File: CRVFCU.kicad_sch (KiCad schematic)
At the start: 161 parts, among them J1 TagConnect_TC2030, J2 Conn_01x02, J3 USB_C_Receptacle_USB2.0_16P, J4 Micro_SD_Card_Det2, J5 Conn_01x02, Q3 DMG2301L, Q4 BC818, Q5 DMG2301L, Q6 DMG2301L, U1 MS5611-01BA, U10 W25Q128JVS, U11 EClamp2515K, U12 ESDALC6V1W5, U13 USBLC6-2SC6, U14 USBLC6-2SC6, U15 MAX17049, U16 SI7232DN-T1, U17 SN74LV1T34DCK, U18 AP63205WU, U2 STM32H747IITx, U3 LIS2MDL, U4 ICM-45686, U5 FXMA108, U7 LDL1117S33R, U8 SI7232DN-T1, U9 USBLC6-4SC6, Y1 ECS-.327-6-34QCS-TR, Y2 ECS-250-10-33B-CKY-TR3, Y3 32.768khz

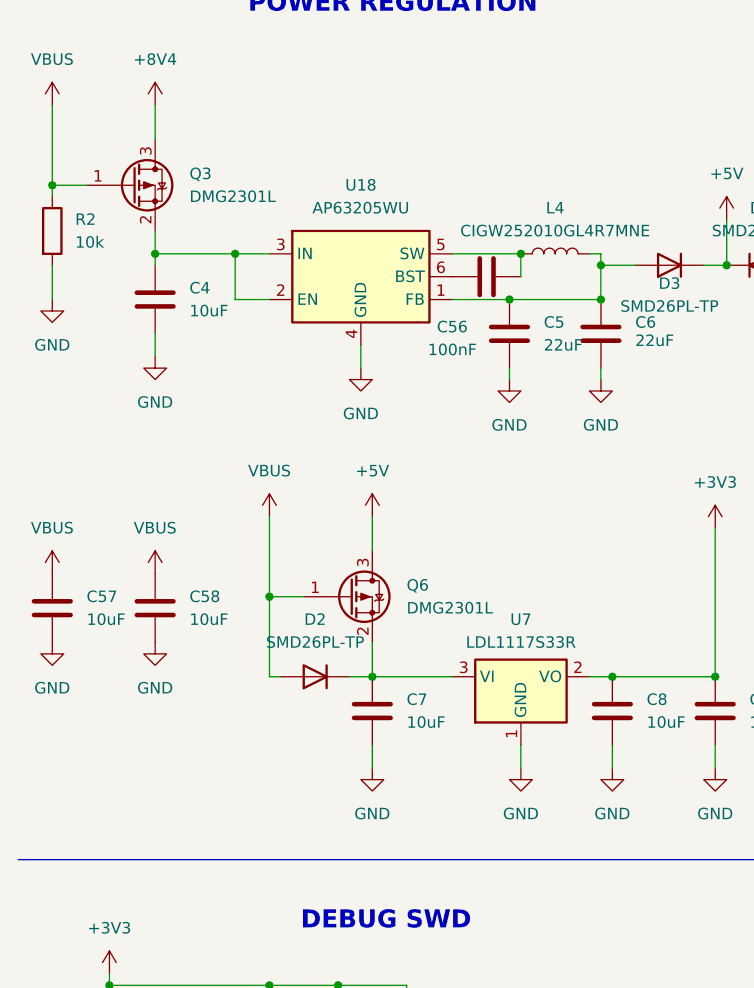
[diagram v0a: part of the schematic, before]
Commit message: changed to higher current mosfet for power supply switching and fixed silkscreens
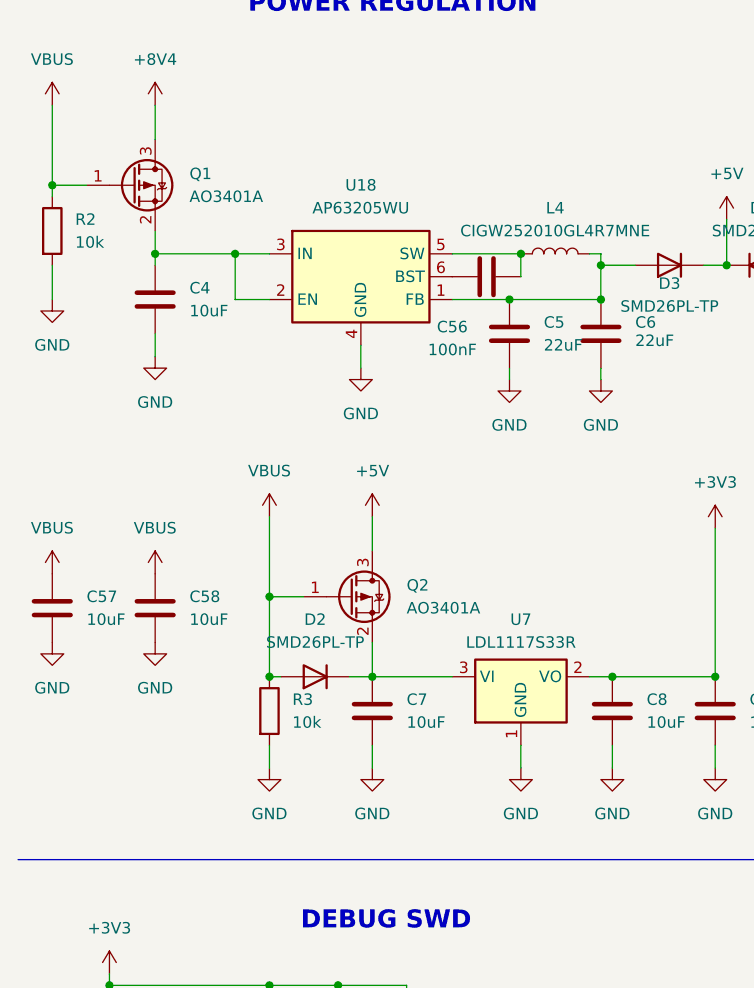
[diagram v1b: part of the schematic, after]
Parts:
- removed Q3, Q6: DMG2301L, Package_TO_SOT_SMD:SOT-23, symbol Transistor_FET:DMG2301L
- added Q1, Q2: AO3401A, Package_TO_SOT_SMD:SOT-23, symbol Transistor_FET:AO3401A
- added R3: 10k, Resistor_SMD:R_0402_1005Metric, symbol Device:R
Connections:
- net +5V: now also Q2.3 (D)
- net +8V4: now also Q1.3 (D)
- net GND: now also R3.2
- net VBUS: now also Q1.1 (G), Q2.1 (G), R3.1
- net at C7.1, D2.1 (K), U7.3 (VI): now also Q2.2 (S)
- net at C4.1, U18.2 (EN), U18.3 (IN): now also Q1.2 (S)
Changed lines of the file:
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@@
 	)
 	(junction
+		(at 40.64 91.44)
+		(diameter 0)
+		(color 0 0 0 0)
+	)
+	(junction
 		(at 196.85 285.75)
 		(diameter 0)
@@
 	(wire
 		(pts
+			(xy 40.64 99.06) (xy 40.64 101.6)
+		)
+		(stroke
+			(width 0)
+			(type default)
+		)
+	)
+	(wire
+		(pts
 			(xy 359.41 102.87) (xy 368.3 102.87)
 		)
@@
 	)
 	(symbol
-		(lib_id "Transistor_FET:DMG2301L")
-		(at 49.53 82.55 0)
-		(unit 1)
-		(exclude_from_sim no)
-		(in_bom yes)
-		(on_board yes)
-		(dnp no)
-		(fields_autoplaced yes)
-		(property "Reference" "Q6"
-			(at 55.88 81.2799 0)
-			(effects
-				(font
-					(size 1.27 1.27)
-				)
-				(justify left)
-			)
-		)
-		(property "Value" "DMG2301L"
-			(at 55.88 83.8199 0)
-			(effects
-				(font
-					(size 1.27 1.27)
-				)
-				(justify left)
-			)
-		)
-		(property "Footprint" "Package_TO_SOT_SMD:SOT-23"
-			(at 54.61 84.455 0)
-			(effects
-				(font
-					(size 1.27 1.27)
-					(italic yes)
-				)
-				(justify left)
-				(hide yes)
-			)
-		)
-		(property "Datasheet" "https://www.diodes.com/assets/Datasheets/DMG2301L.pdf"
-			(at 54.61 86.36 0)
-			(effects
-				(font
-					(size 1.27 1.27)
-				)
-				(justify left)
-				(hide yes)
-			)
-		)
-		(property "Description" "-3A Id, -20V Vds, P-Channel MOSFET, SOT-23"
-			(at 49.53 82.55 0)
-			(effects
-				(font
-					(size 1.27 1.27)
-				)
-				(hide yes)
-			)
-		)
-		(pin "1"
-		)
-		(pin "2"
-		)
-		(pin "3"
-		)
-		(instances
-			(project "CRVFCU"
-				(path "/ad8e65f5-b3fb-4c85-9d9e-17b5feb23144"
-					(reference "Q6")
-					(unit 1)
-				)
-			)
-		)
-	)
-	(symbol
 		(lib_id "Device:R")
 		(at 284.48 335.28 90)
@@
 		(on_board yes)
 		(dnp no)
-		(fields_autoplaced yes)
 		(property "Reference" "D2"
 			(at 45.72 85.09 0)
@@
 	)
 	(symbol
+		(lib_id "Transistor_FET:AO3401A")
+		(at 25.4 36.83 0)
+		(unit 1)
+		(exclude_from_sim no)
+		(in_bom yes)
+		(on_board yes)
+		(dnp no)
+		(fields_autoplaced yes)
+		(property "Reference" "Q1"
+			(at 31.75 35.5599 0)
+			(effects
+				(font
+					(size 1.27 1.27)
+				)
+				(justify left)
+			)
+		)
+		(property "Value" "AO3401A"
+			(at 31.75 38.0999 0)
+			(effects
+				(font
+					(size 1.27 1.27)
+				)
+				(justify left)
+			)
+		)
+		(property "Footprint" "Package_TO_SOT_SMD:SOT-23"
+			(at 30.48 38.735 0)
+			(effects
+				(font
+					(size 1.27 1.27)
+					(italic yes)
+				)
+				(justify left)
+				(hide yes)
+			)
+		)
+		(property "Datasheet" "http://www.aosmd.com/pdfs/datasheet/AO3401A.pdf"
+			(at 30.48 40.64 0)
+			(effects
+				(font
+					(size 1.27 1.27)
+				)
+				(justify left)
+				(hide yes)
+			)
+		)
+		(property "Description" "-4.0A Id, -30V Vds, P-Channel MOSFET, SOT-23"
+			(at 25.4 36.83 0)
+			(effects
+				(font
+					(size 1.27 1.27)
+				)
+				(hide yes)
+			)
+		)
+		(pin "1"
+		)
+		(pin "3"
+		)
+		(pin "2"
+		)
+		(instances
+			(project ""
+				(path "/ad8e65f5-b3fb-4c85-9d9e-17b5feb23144"
+					(reference "Q1")
+					(unit 1)
+				)
+			)
+		)
+	)
+	(symbol
 		(lib_id "Device:C")
 		(at 134.62 243.84 0)
@@
 	)
 	(symbol
-		(lib_id "Transistor_FET:DMG2301L")
-		(at 25.4 36.83 0)
-		(unit 1)
-		(exclude_from_sim no)
-		(in_bom yes)
-		(on_board yes)
-		(dnp no)
-		(fields_autoplaced yes)
-		(property "Reference" "Q3"
-			(at 31.75 35.5599 0)
-			(effects
-				(font
-					(size 1.27 1.27)
-				)
-				(justify left)
-			)
-		)
-		(property "Value" "DMG2301L"
-			(at 31.75 38.0999 0)
-			(effects
-				(font
-					(size 1.27 1.27)
-				)
-				(justify left)
-			)
-		)
-		(property "Footprint" "Package_TO_SOT_SMD:SOT-23"
-			(at 30.48 38.735 0)
-			(effects
-				(font
-					(size 1.27 1.27)
-					(italic yes)
-				)
-				(justify left)
-				(hide yes)
-			)
-		)
-		(property "Datasheet" "https://www.diodes.com/assets/Datasheets/DMG2301L.pdf"
-			(at 30.48 40.64 0)
-			(effects
-				(font
-					(size 1.27 1.27)
-				)
-				(justify left)
-				(hide yes)
-			)
-		)
-		(property "Description" "-3A Id, -20V Vds, P-Channel MOSFET, SOT-23"
-			(at 25.4 36.83 0)
-			(effects
-				(font
-					(size 1.27 1.27)
-				)
-				(hide yes)
-			)
-		)
-		(pin "1"
-		)
-		(pin "2"
-		)
-		(pin "3"
-		)
-		(instances
-			(project "CRVFCU"
-				(path "/ad8e65f5-b3fb-4c85-9d9e-17b5feb23144"
-					(reference "Q3")
-					(unit 1)
-				)
-			)
-		)
-	)
-	(symbol
 		(lib_id "Device:C")
 		(at 293.37 73.66 0)
@@
 	(symbol
 		(lib_id "Device:R")
+		(at 40.64 95.25 0)
+		(unit 1)
+		(exclude_from_sim no)
+		(in_bom yes)
+		(on_board yes)
+		(dnp no)
+		(fields_autoplaced yes)
+		(property "Reference" "R3"
+			(at 43.18 93.9799 0)
+			(effects
+				(font
+					(size 1.27 1.27)
+				)
+				(justify left)
+			)
+		)
+		(property "Value" "10k"
+			(at 43.18 96.5199 0)
+			(effects
+				(font
+					(size 1.27 1.27)
+				)
+				(justify left)
+			)
+		)
+		(property "Footprint" "Resistor_SMD:R_0402_1005Metric"
+			(at 38.862 95.25 90)
+			(effects
+				(font
+					(size 1.27 1.27)
+				)
+				(hide yes)
+			)
+		)
+		(property "Datasheet" "~"
+			(at 40.64 95.25 0)
+			(effects
+				(font
+					(size 1.27 1.27)
+				)
+				(hide yes)
+			)
+		)
+		(property "Description" "Resistor"
+			(at 40.64 95.25 0)
+			(effects
+				(font
+					(size 1.27 1.27)
+				)
+				(hide yes)
+			)
+		)
+		(pin "1"
+		)
+		(pin "2"
+		)
+		(instances
+			(project "CRVFCU"
+				(path "/ad8e65f5-b3fb-4c85-9d9e-17b5feb23144"
+					(reference "R3")
+					(unit 1)
+				)
+			)
+		)
+	)
+	(symbol
+		(lib_id "Device:R")
 		(at 281.94 86.36 0)
 		(unit 1)
@@
 	)
 	(symbol
+		(lib_id "Transistor_FET:AO3401A")
+		(at 49.53 82.55 0)
+		(unit 1)
+		(exclude_from_sim no)
+		(in_bom yes)
+		(on_board yes)
+		(dnp no)
+		(fields_autoplaced yes)
+		(property "Reference" "Q2"
+			(at 55.88 81.2799 0)
+			(effects
+				(font
+					(size 1.27 1.27)
+				)
+				(justify left)
+			)
+		)
+		(property "Value" "AO3401A"
+			(at 55.88 83.8199 0)
+			(effects
+				(font
+					(size 1.27 1.27)
+				)
+				(justify left)
+			)
+		)
+		(property "Footprint" "Package_TO_SOT_SMD:SOT-23"
+			(at 54.61 84.455 0)
+			(effects
+				(font
+					(size 1.27 1.27)
+					(italic yes)
+				)
+				(justify left)
+				(hide yes)
+			)
+		)
+		(property "Datasheet" "http://www.aosmd.com/pdfs/datasheet/AO3401A.pdf"
+			(at 54.61 86.36 0)
+			(effects
+				(font
+					(size 1.27 1.27)
+				)
+				(justify left)
+				(hide yes)
+			)
+		)
+		(property "Description" "-4.0A Id, -30V Vds, P-Channel MOSFET, SOT-23"
+			(at 49.53 82.55 0)
+			(effects
+				(font
+					(size 1.27 1.27)
+				)
+				(hide yes)
+			)
+		)
+		(pin "1"
+		)
+		(pin "3"
+		)
+		(pin "2"
+		)
+		(instances
+			(project "CRVFCU"
+				(path "/ad8e65f5-b3fb-4c85-9d9e-17b5feb23144"
+					(reference "Q2")
+					(unit 1)
+				)
+			)
+		)
+	)
+	(symbol
 		(lib_id "power:VBUS")
 		(at 99.06 24.13 0)
@@
 					(unit 1)
 				)
+			)
+		)
+	)
+	(symbol
+		(lib_id "power:GND")
+		(at 40.64 101.6 0)
+		(unit 1)
+		(exclude_from_sim no)
+		(in_bom yes)
+		(on_board yes)
+		(dnp no)
+		(fields_autoplaced yes)
+		(property "Reference" "#PWR0162"
+			(at 40.64 107.95 0)
+			(effects
+				(font
+					(size 1.27 1.27)
+				)
+				(hide yes)
+			)
+		)
+		(property "Value" "GND"
+			(at 40.64 106.68 0)
+			(effects
+				(font
+					(size 1.27 1.27)
+				)
+			)
+		)
+		(property "Footprint" ""
+			(at 40.64 101.6 0)
+			(effects
+				(font
+					(size 1.27 1.27)
+				)
+				(hide yes)
+			)
+		)
+		(property "Datasheet" ""
+			(at 40.64 101.6 0)
+			(effects
+				(font
+					(size 1.27 1.27)
+				)
+				(hide yes)
+			)
+		)
+		(property "Description" "Power symbol creates a global label with name \"GND\" , ground"
+			(at 40.64 101.6 0)
+			(effects
+				(font
+					(size 1.27 1.27)
+				)
+				(hide yes)
+			)
+		)
+		(pin "1"
+		)
+		(instances
+			(project "CRVFCU"
+				(path "/ad8e65f5-b3fb-4c85-9d9e-17b5feb23144"
+					(reference "#PWR0162")
+					(unit 1)
+				)

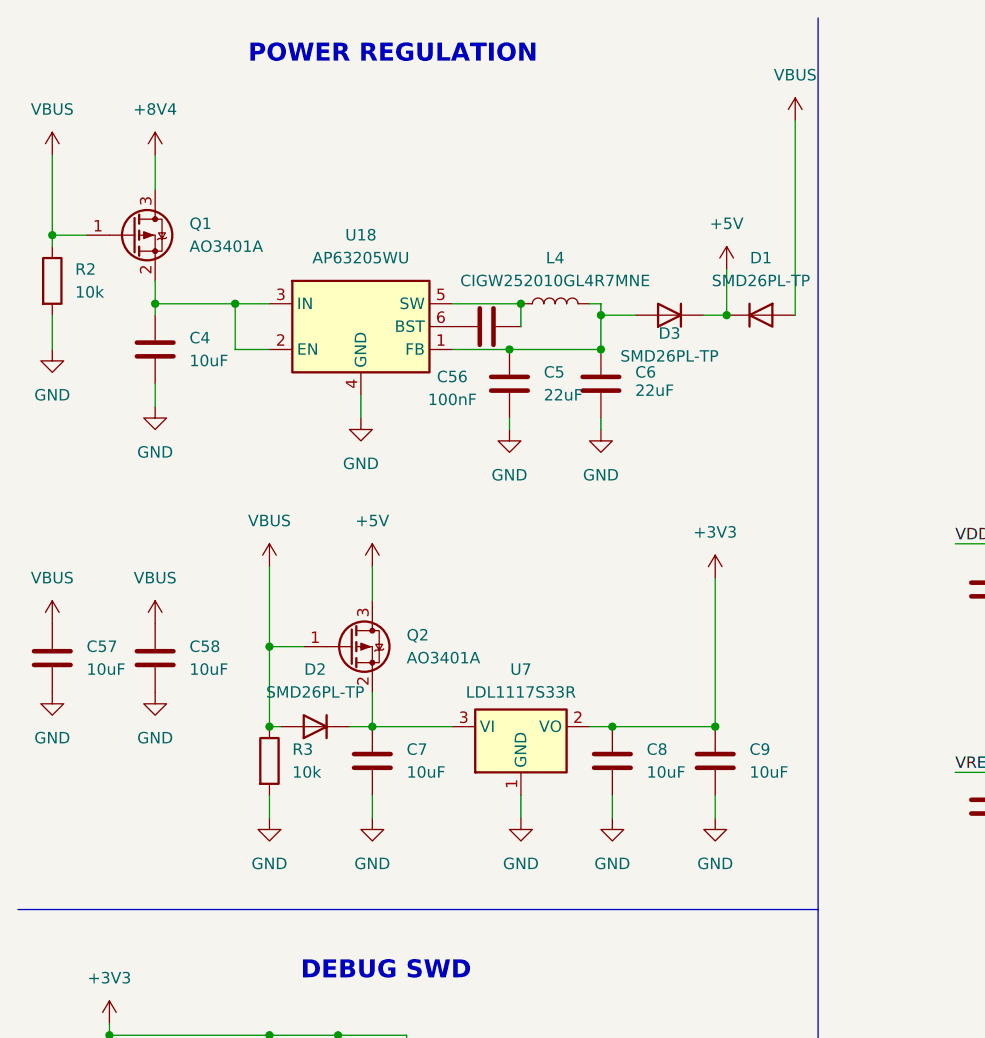
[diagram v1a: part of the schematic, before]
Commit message: simplified power delivery
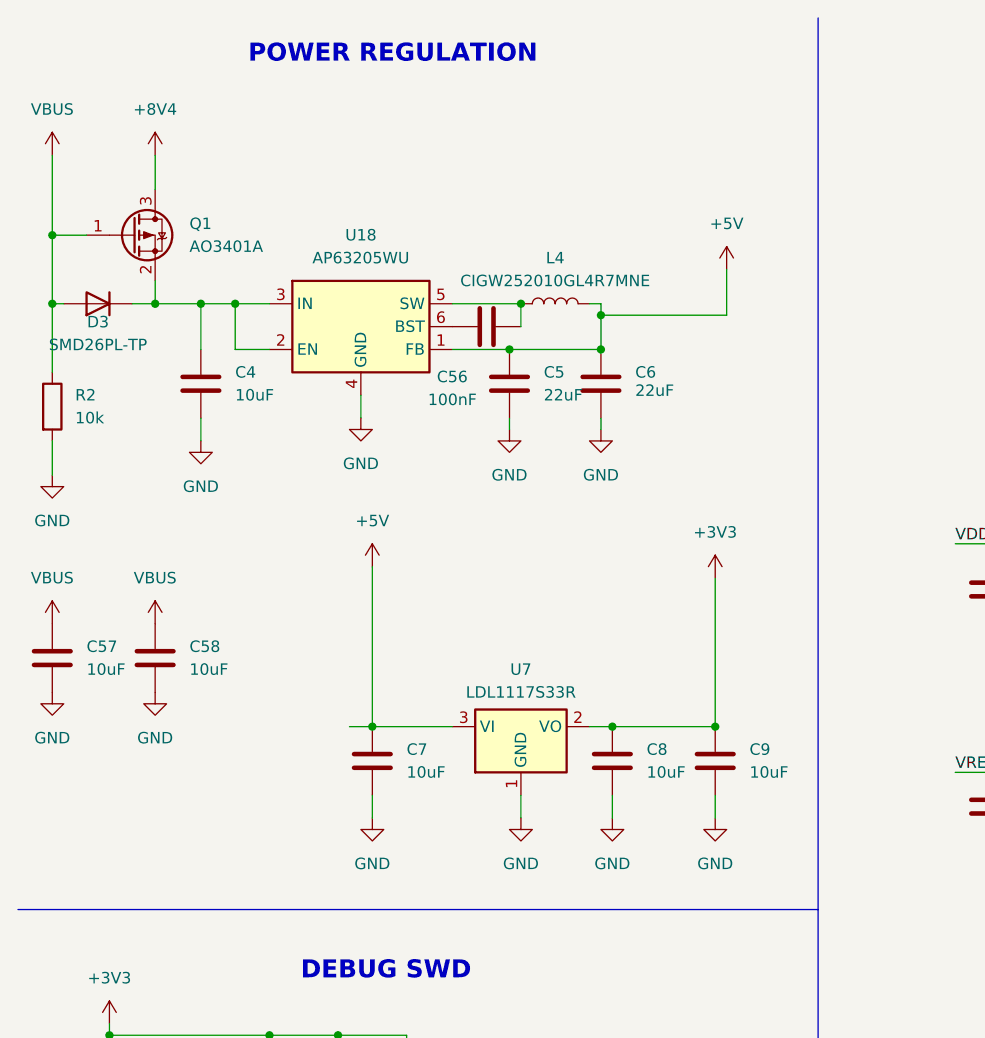
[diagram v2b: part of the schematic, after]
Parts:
- removed D1, D2: SMD26PL-TP, Diode_SMD:D_SOD-123F, symbol Device:D
- removed Q2: AO3401A, Package_TO_SOT_SMD:SOT-23, symbol Transistor_FET:AO3401A
- removed R3: 10k, Resistor_SMD:R_0402_1005Metric, symbol Device:R
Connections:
- net +5V: now also C5.1, C6.1, C7.1, L4.2, U18.1 (FB), U7.3 (VI); no longer D3.1 (K)
- net VBUS: now also D3.2 (A)
- net at C4.1, Q1.2 (S), U18.2 (EN)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: now also D3.1 (K)
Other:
- moved on the sheet: C4, D3, R2

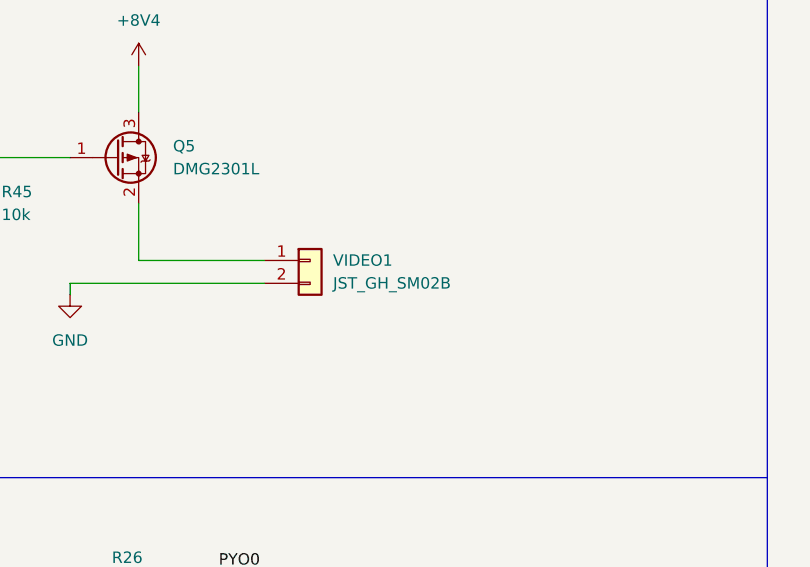
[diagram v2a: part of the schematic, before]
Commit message: changed cam to jst ph
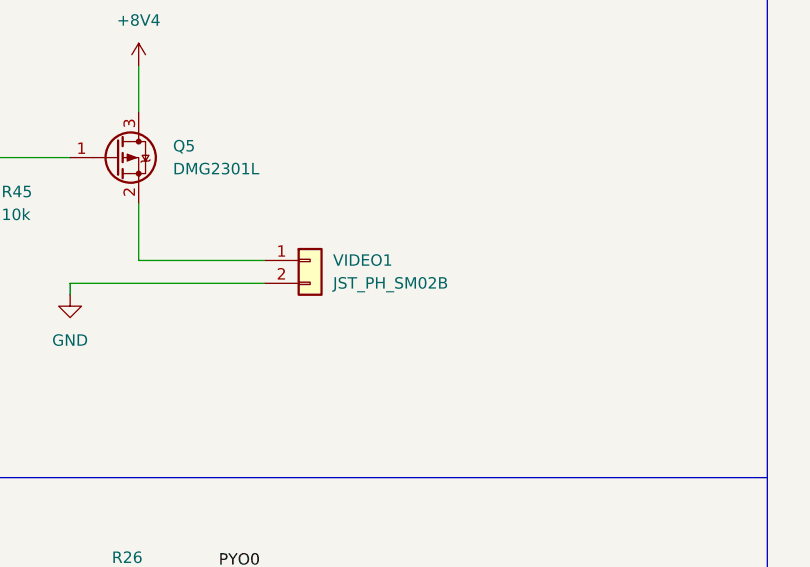
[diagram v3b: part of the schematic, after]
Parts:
- VIDEO1: value JST_GH_SM02B -> JST_PH_SM02B; footprint Connector_JST:JST_GH_SM02B-GHS-TB_1x02-1MP_P1.25mm_Horizontal -> Connector_JST:JST_PH_B2B-PH-K_1x02_P2.00mm_Vertical
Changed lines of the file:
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@@
 			)
 		)
-		(property "Value" "JST_GH_SM02B"
+		(property "Value" "JST_PH_SM02B"
 			(at 383.54 298.4499 0)
 			(effects
@@
 			)
 		)
-		(property "Footprint" "Connector_JST:JST_GH_SM02B-GHS-TB_1x02-1MP_P1.25mm_Horizontal"
+		(property "Footprint" "Connector_JST:JST_PH_B2B-PH-K_1x02_P2.00mm_Vertical"
 			(at 381 295.91 0)
 			(effects
